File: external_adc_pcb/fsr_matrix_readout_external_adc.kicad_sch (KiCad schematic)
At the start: 6 parts

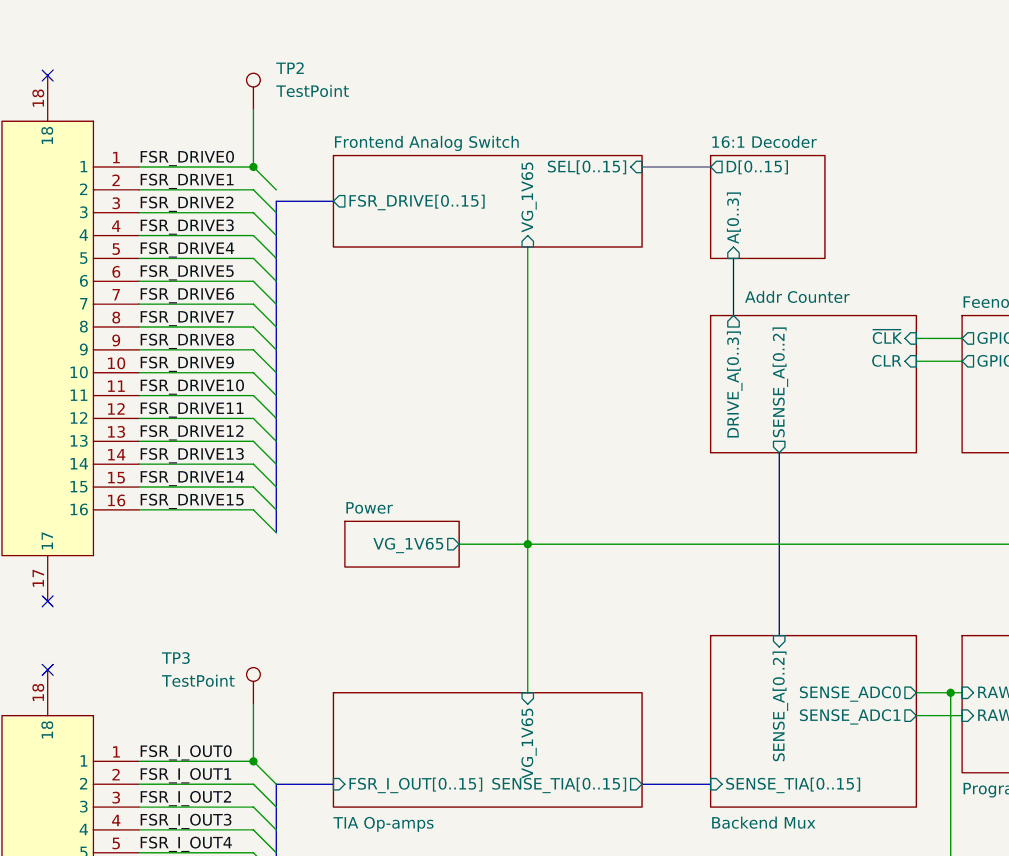
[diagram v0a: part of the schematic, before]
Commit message: done schematics for internal ADC version
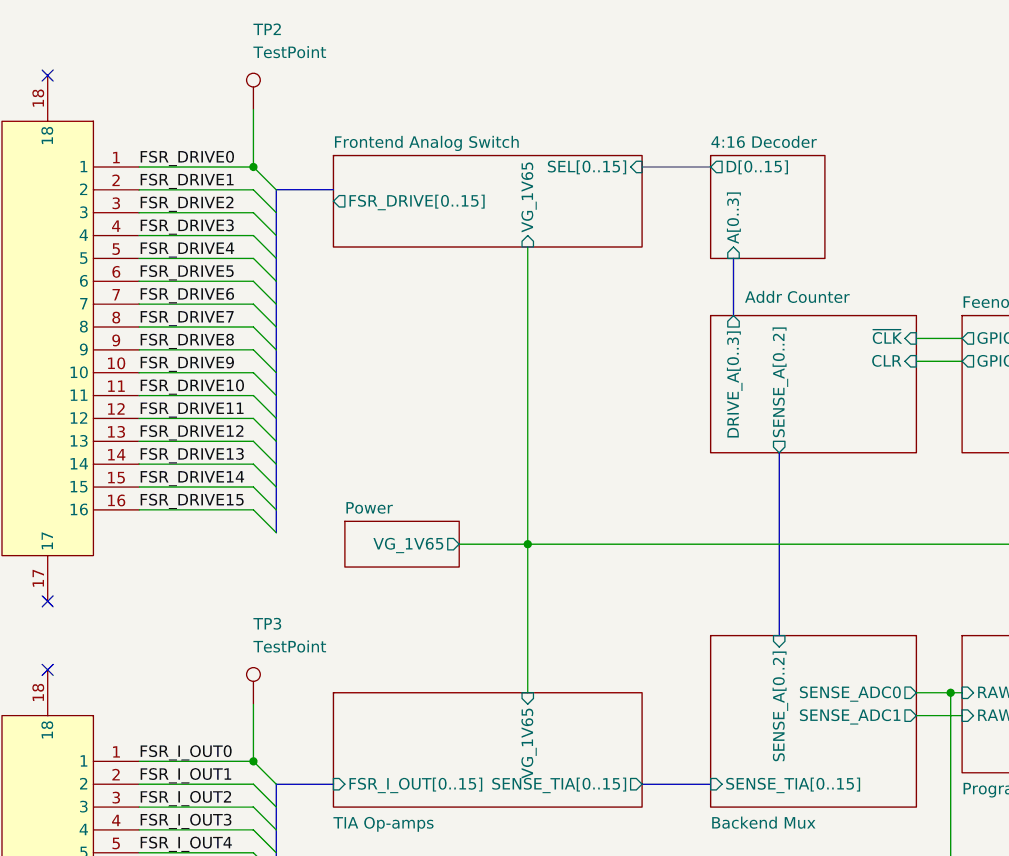
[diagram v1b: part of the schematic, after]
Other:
- sheet 16:1 Decoder renamed 4:16 Decoder
- sheet 4:16 Decoder: file 16_to_1_decoder.kicad_sch -> 4_to_16_decoder.kicad_sch
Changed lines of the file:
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@@
 	(bus
 		(pts
-			(xy 106.68 60.96) (xy 100.33 60.96)
+			(xy 106.68 59.69) (xy 100.33 59.69)
 		)
 		(stroke
@@
 	(bus
 		(pts
-			(xy 100.33 60.96) (xy 100.33 62.23)
+			(xy 100.33 59.69) (xy 100.33 62.23)
 		)
 		(stroke
@@
 		(dnp no)
 		(property "Reference" "TP3"
-			(at 87.63 111.76 0)
+			(at 97.79 107.95 0)
 			(show_name no)
 			(do_not_autoplace no)
@@
 		)
 		(property "Value" "TestPoint"
-			(at 87.63 114.3 0)
+			(at 97.79 110.49 0)
 			(show_name no)
 			(do_not_autoplace no)
@@
 		(dnp no)
 		(property "Reference" "TP2"
-			(at 100.33 46.2279 0)
+			(at 97.79 41.91 0)
 			(show_name no)
 			(do_not_autoplace no)
@@
 		)
 		(property "Value" "TestPoint"
-			(at 100.33 48.7679 0)
+			(at 97.79 44.45 0)
 			(show_name no)
 			(do_not_autoplace no)
@@
 			(color 0 0 0 0)
 		)
-		(property "Sheetname" "16:1 Decoder"
+		(property "Sheetname" "4:16 Decoder"
 			(at 148.59 55.1684 0)
 			(show_name no)
@@
 			)
 		)
-		(property "Sheetfile" "16_to_1_decoder.kicad_sch"
+		(property "Sheetfile" "4_to_16_decoder.kicad_sch"
 			(at 148.59 51.308 0)
 			(hide yes)

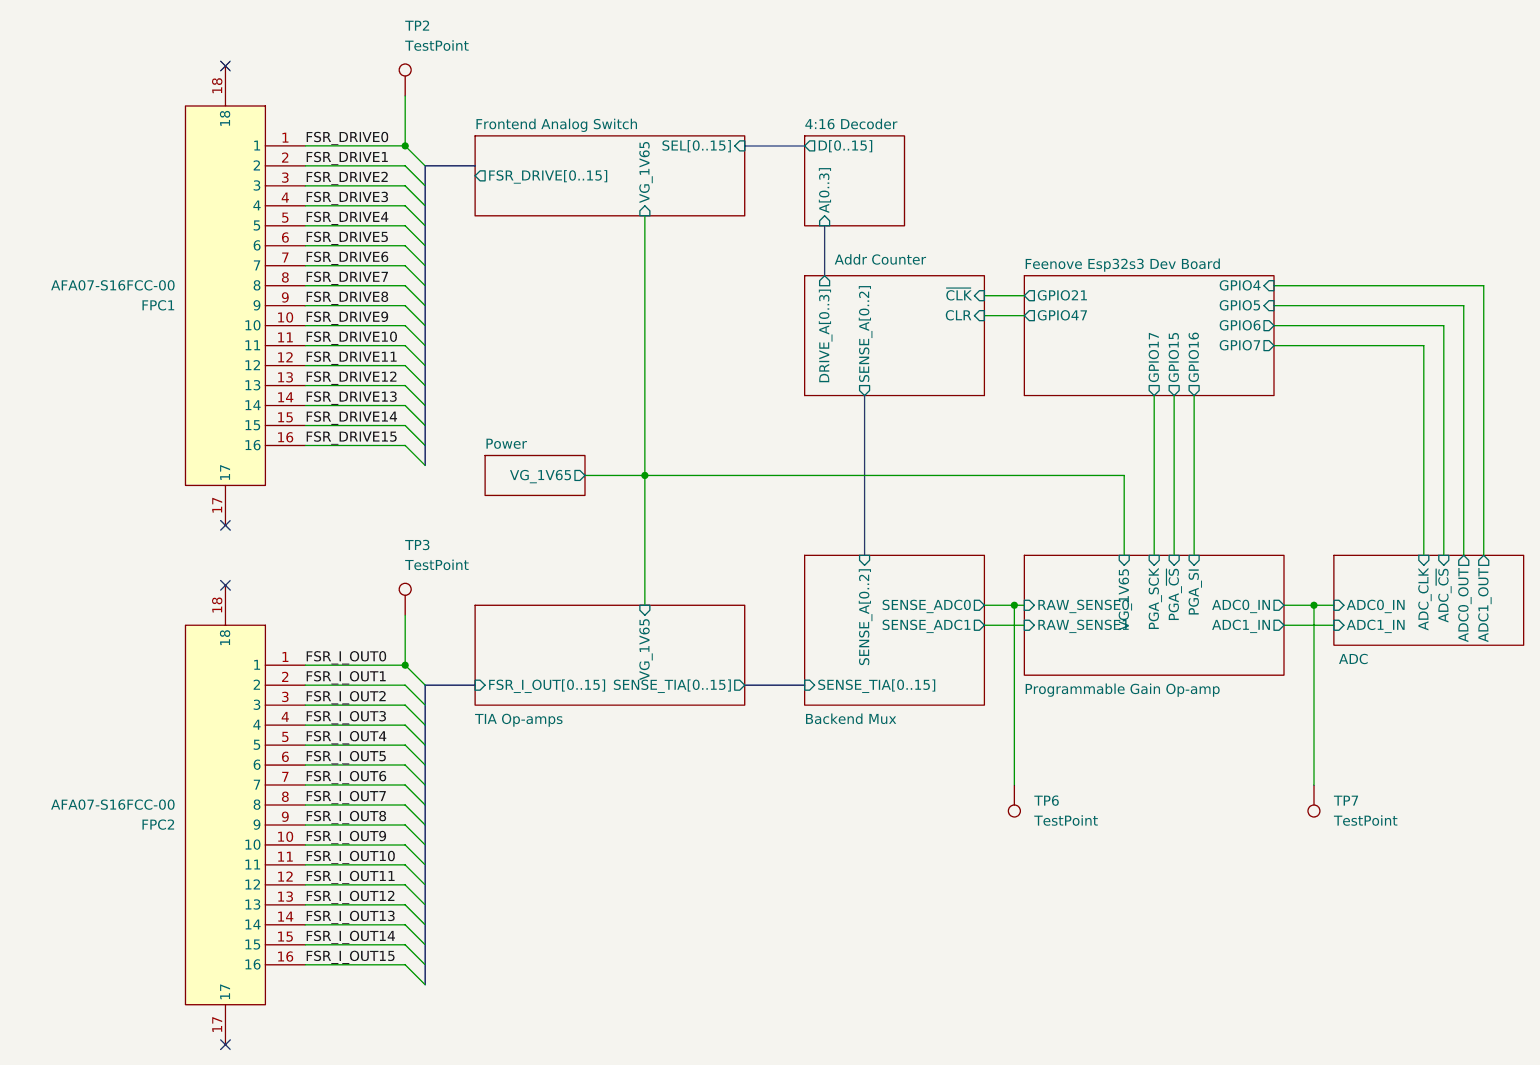
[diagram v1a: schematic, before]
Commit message: adjust VG issue for internal ADC version; changed naming for VG
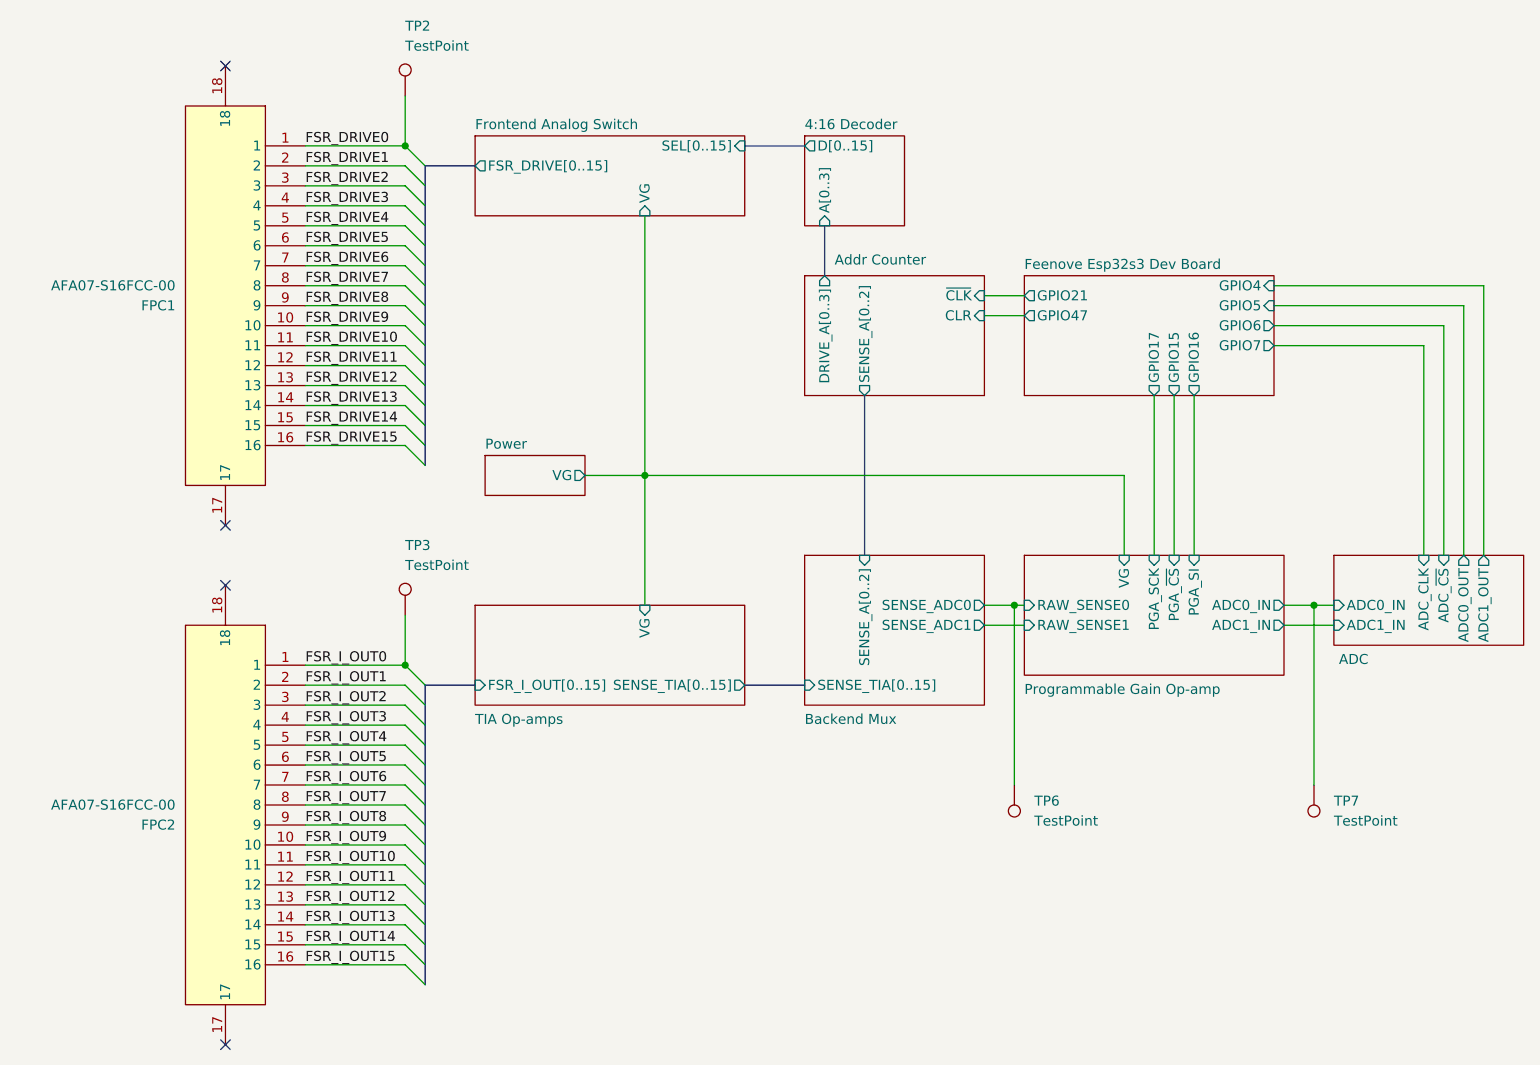
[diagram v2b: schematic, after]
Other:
- sheet Frontend Analog Switch ports: added VG; removed VG_1V65
- sheet Power ports: added VG; removed VG_1V65
- sheet Programmable Gain Op-amp ports: added VG; removed VG_1V65
- sheet TIA Op-amps ports: added VG; removed VG_1V65
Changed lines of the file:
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@@
 			)
 		)
-		(pin "VG_1V65" input
+		(pin "VG" input
 			(at 128.27 66.04 270)
 			(effects
@@
 		)
 		(pin "FSR_DRIVE[0..15]" output
-			(at 106.68 60.96 180)
+			(at 106.68 59.69 180)
 			(effects
 				(font
@@
 			)
 		)
-		(pin "VG_1V65" output
+		(pin "VG" output
 			(at 120.65 99.06 0)
 			(effects
@@
 			)
 		)
-		(pin "VG_1V65" input
+		(pin "VG" input
 			(at 128.27 115.57 90)
 			(effects
@@
 			)
 		)
-		(pin "VG_1V65" input
+		(pin "VG" input
 			(at 189.23 109.22 90)
 			(effects
